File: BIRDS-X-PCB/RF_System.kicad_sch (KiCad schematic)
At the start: 44 parts, among them J1 SJ-43515TS, Q1 2N7000, Q2 2N7000, SW1 PTS645VL58-2 LFS, U1 MCP6004, U2 24LC32

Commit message: Clean up NucleoTNC
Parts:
- removed A1: NUCLEO-L432KC, KiCAD:MODULE_NUCLEO-L432KC, symbol NUCLEO-F303K8:NUCLEO-F303K8
- removed C10, C11: 0.1uF, Capacitor_THT:C_Disc_D3.4mm_W2.1mm_P2.50mm, symbol Device:C
- removed C12: 1uF, Capacitor_THT:C_Disc_D6.0mm_W2.5mm_P5.00mm, symbol Device:C
- removed C13: 10uF, Capacitor_THT:C_Disc_D6.0mm_W2.5mm_P5.00mm, symbol Device:C
- removed C3: 10nF, Capacitor_THT:C_Disc_D6.0mm_W2.5mm_P5.00mm, symbol Device:C
- removed C4, C9: 470pF, Capacitor_THT:C_Disc_D6.0mm_W2.5mm_P5.00mm, symbol Device:C
- removed C5, C8: 33nF, Capacitor_THT:C_Disc_D6.0mm_W2.5mm_P5.00mm, symbol Device:C
- removed H1, H2, H3, H4: MountingHole_Pad, MountingHole:MountingHole_3.2mm_M3_ISO14580_Pad, symbol Mechanical:MountingHole_Pad
- removed J1: SJ-43515TS, KiCAD:CUI_SJ-43515TS, symbol Connector:AudioJack4
- removed R10, R15: 16K, Resistor_THT:R_Axial_DIN0207_L6.3mm_D2.5mm_P7.62mm_Horizontal, symbol Device:R
- removed R12, R14: 510, Resistor_THT:R_Axial_DIN0207_L6.3mm_D2.5mm_P7.62mm_Horizontal, symbol Device:R
- removed R13, R6: 220, Resistor_THT:R_Axial_DIN0207_L6.3mm_D2.5mm_P7.62mm_Horizontal, symbol Device:R
- removed R16, R7: 30K, Resistor_THT:R_Axial_DIN0207_L6.3mm_D2.5mm_P7.62mm_Horizontal, symbol Device:R
- removed R17, R18, R4: 2K2, Resistor_THT:R_Axial_DIN0207_L6.3mm_D2.5mm_P7.62mm_Horizontal, symbol Device:R
- removed R2, R3: R470, Resistor_THT:R_Axial_DIN0207_L6.3mm_D2.5mm_P7.62mm_Horizontal, symbol Device:R
- removed R9: 100K, Resistor_THT:R_Axial_DIN0207_L6.3mm_D2.5mm_P7.62mm_Horizontal, symbol Device:R
- removed SW1: PTS645VL58-2 LFS, Button_Switch_THT:SW_Tactile_SPST_Angled_PTS645Vx58-2LFS, symbol Switch:SW_Push
- added C405 (x2): 33n, Capacitor_SMD:C_0603_1608Metric_Pad1.08x0.95mm_HandSolder, symbol Device:C
- added C405 (x2): 100n, Capacitor_SMD:C_0603_1608Metric_Pad1.08x0.95mm_HandSolder, symbol Device:C
- added C405: 10n, Capacitor_SMD:C_0603_1608Metric_Pad1.08x0.95mm_HandSolder, symbol Device:C
- added C405 (x2): 470p, Capacitor_SMD:C_0603_1608Metric_Pad1.08x0.95mm_HandSolder, symbol Device:C
- added R403 (x2): 30k, Resistor_SMD:R_0603_1608Metric_Pad0.98x0.95mm_HandSolder, symbol Device:R
- added R403 (x2): 470, Resistor_SMD:R_0603_1608Metric_Pad0.98x0.95mm_HandSolder, symbol Device:R
- added R403 (x2): 510, Resistor_SMD:R_0603_1608Metric_Pad0.98x0.95mm_HandSolder, symbol Device:R
- added R403 (x2): 16k, Resistor_SMD:R_0603_1608Metric_Pad0.98x0.95mm_HandSolder, symbol Device:R
- added R403: 100k, Resistor_SMD:R_0603_1608Metric_Pad0.98x0.95mm_HandSolder, symbol Device:R
- added R403: 2.2k, Resistor_SMD:R_0603_1608Metric_Pad0.98x0.95mm_HandSolder, symbol Device:R
- added R403 (x2): 220, Resistor_SMD:R_0603_1608Metric_Pad0.98x0.95mm_HandSolder, symbol Device:R
- U2: value 24LC32 -> 24LC32A/SN; footprint Package_DIP:DIP-8_W7.62mm_Socket -> Package_SO:SOP-8_3.9x4.9mm_P1.27mm; LCSC (none) -> C615215
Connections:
- net +3.3V: now also C405.1, C405.1
- net ADC_AUDIO: now also C405.1, R403.2
- net AUDIO_OUT: now also R403.1
- net DAC_AUDIO: now also R403.2
- net GND: now also C405.2, C405.2, C405.2, C405.2, C405.2, C405.2, C405.2
- net PTT_MULTIPLEX: now also R403.2
- net PTT_SIMPLEX: now also R403.2
- net at C7.1: now also R403.1, R403.2
- net at U1.3 (+): now also C405.1, R403.1
- net at C7.2, U1.1, U1.2 (-): now also R403.2
- net at C6.1, U1.13 (-), U1.14: now also R403.1
- net at U1.12 (+): now also C405.1, R403.2
- net at U1.8, U1.9 (-): now also R403.1
- net at Q2.2 (G), R11.1: now also R403.1
- net at Q1.3 (D): now also R403.2
- net at C6.2: now also R403.1, R403.2
- net at C2.2: now also R403.1
- net at R8.1, U1.5 (+): now also R403.1
- net at U1.6 (-), U1.7: now also R403.1, R403.2
- net at Q1.2 (G), R5.1: now also R403.1
- new net: C405.1, R403.2
- new net: C405.1, R403.1, R403.2
- no-connect marks 15 -> 0
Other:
- note added: "PERSISTENT CONFIGURATION - EEPROM"
- note added: "PTT = Push-to-Talk"
- note added: "TODO confirm if PTT is active high or low"
- note removed: "PERSISTENT CONFIGURATION"
- moved on the sheet: C2, C7, Q1, Q2, R11, R5, R8, U1A, U1B, U2

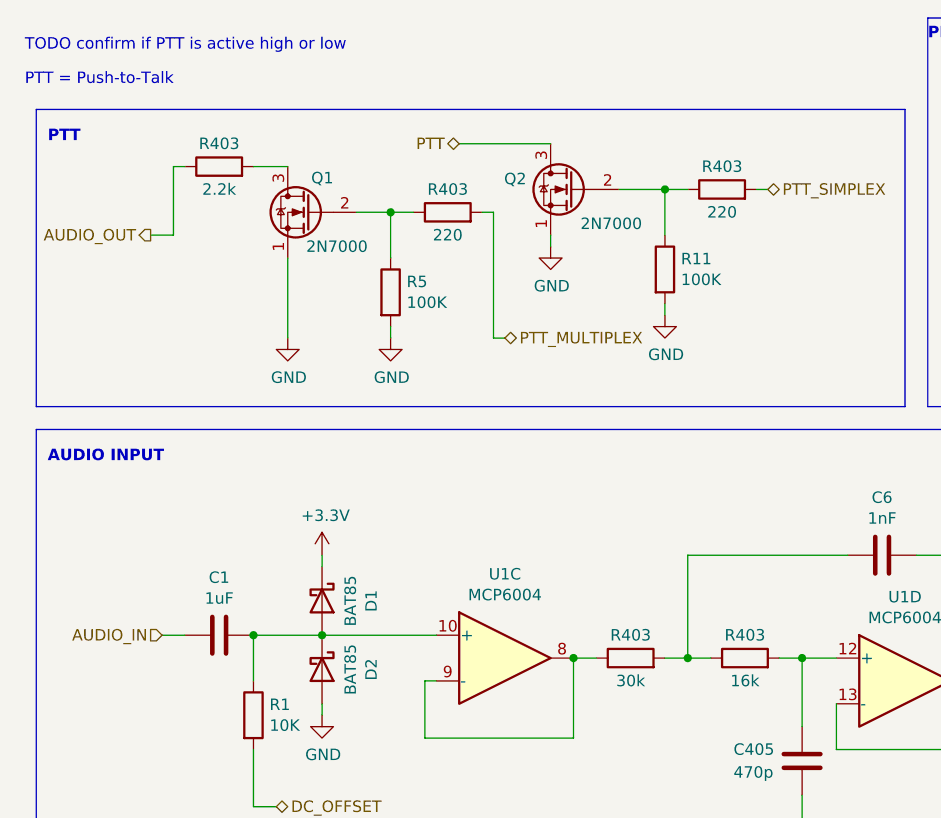
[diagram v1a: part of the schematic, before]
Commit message: Update parts in RF system
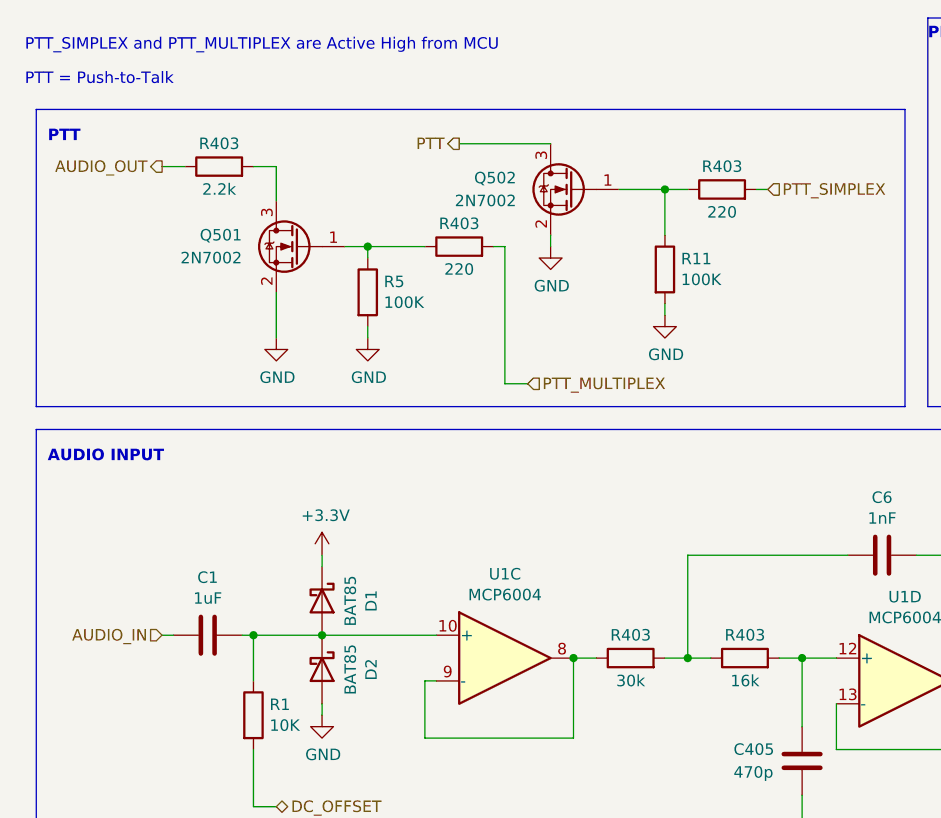
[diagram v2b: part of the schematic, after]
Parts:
- removed Q1, Q2: 2N7000, Package_TO_SOT_THT:TO-92_Inline, symbol Transistor_FET:2N7000
- added Q501, Q502: 2N7002, Package_TO_SOT_THT:TO-92_Inline, symbol Transistor_FET:2N7002
- C1, C2, C6, C7: footprint Capacitor_THT:C_Disc_D6.0mm_W2.5mm_P5.00mm -> Capacitor_SMD:C_0603_1608Metric_Pad1.08x0.95mm_HandSolder
- R1, R11, R5, R8: footprint Resistor_THT:R_Axial_DIN0207_L6.3mm_D2.5mm_P7.62mm_Horizontal -> Resistor_SMD:R_0603_1608Metric_Pad0.98x0.95mm_HandSolder
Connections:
- net GND: now also Q501.2 (S), Q502.2 (S)
- net PTT: now also Q502.3 (D)
- net at R11.1, R403.1: now also Q502.1 (G)
- net at R403.2: now also Q501.3 (D)
- net at R403.1, R5.1: now also Q501.1 (G)
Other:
- note added: "PTT_SIMPLEX and PTT_MULTIPLEX are Active High from MCU"
- note removed: "TODO confirm if PTT is active high or low"
- moved on the sheet: C1, R403, R5

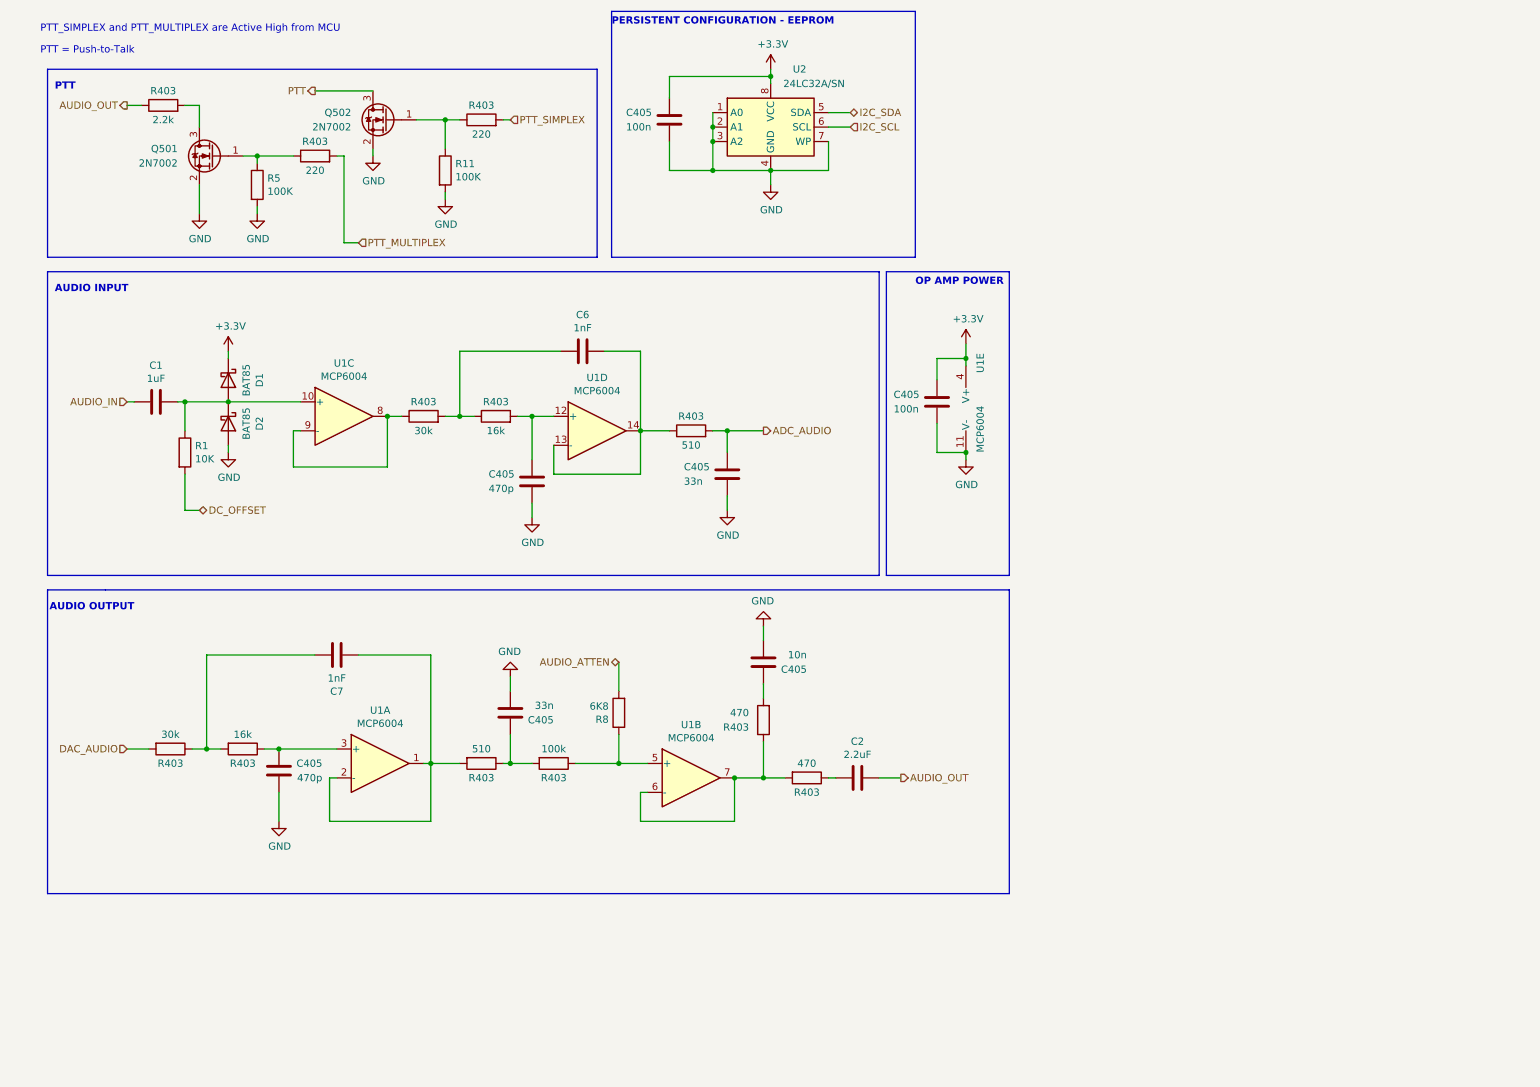
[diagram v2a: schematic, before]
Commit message: Add DRA818V content
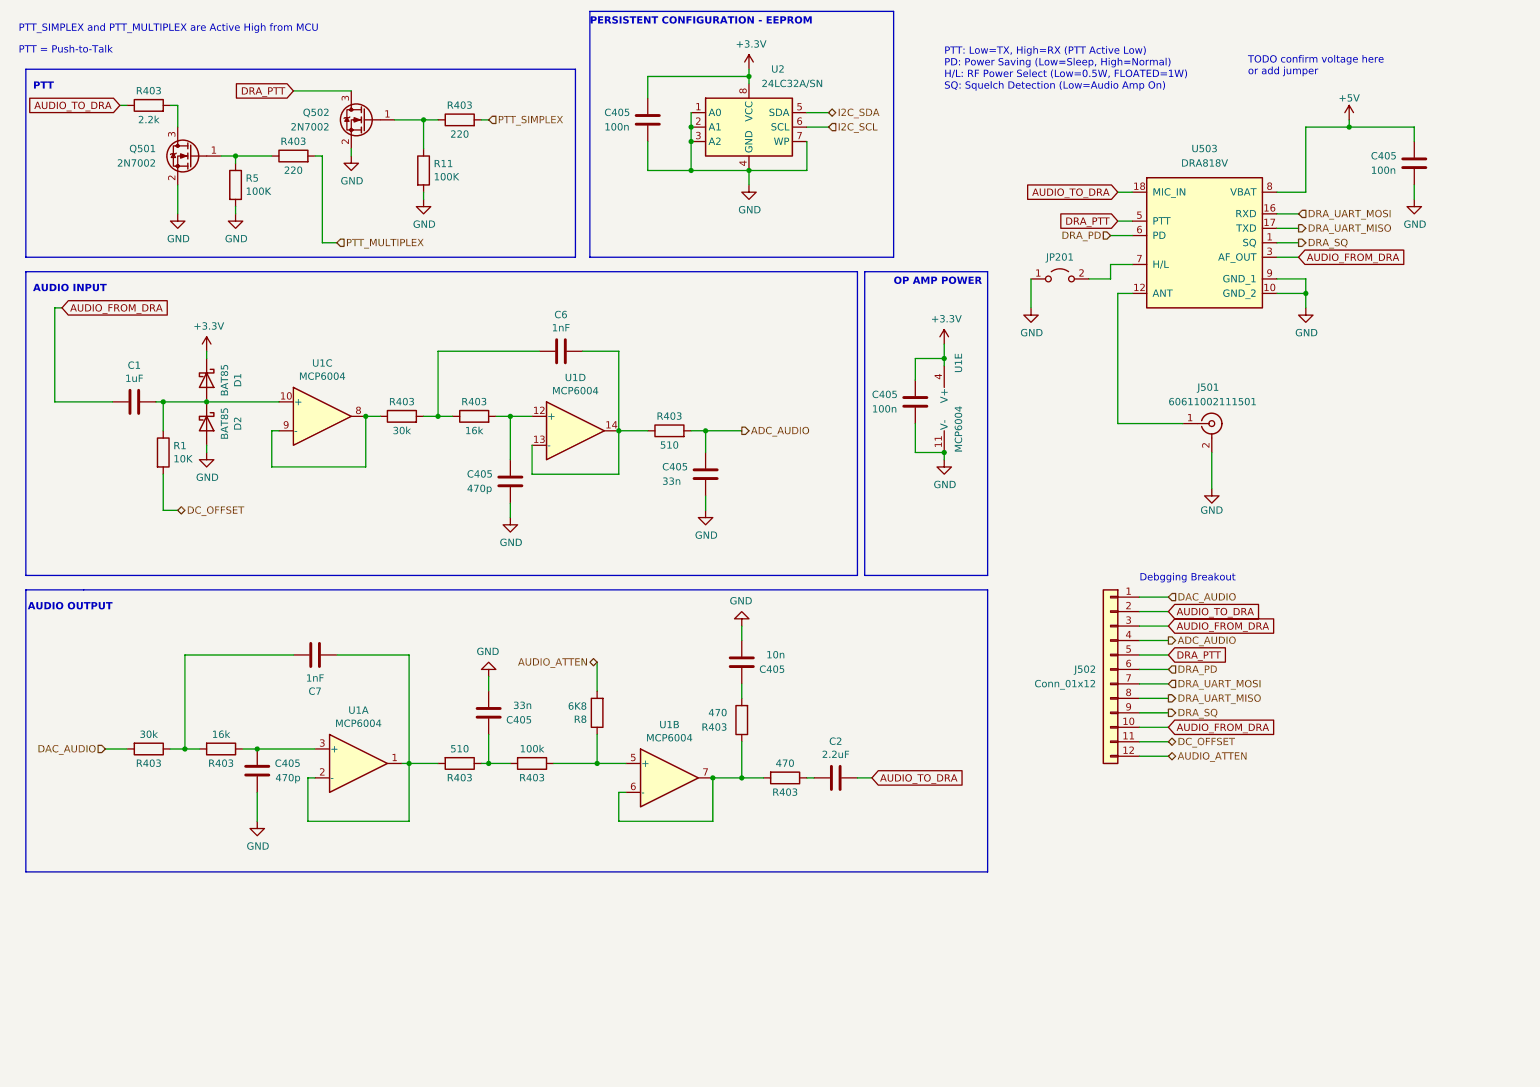
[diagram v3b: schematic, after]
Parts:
- added C405: 100n, Capacitor_SMD:C_0603_1608Metric_Pad1.08x0.95mm_HandSolder, symbol Device:C
- added J501: 60611002111501, Connector_Coaxial:SMA_Amphenol_901-143_Horizontal, symbol Connector:Conn_Coaxial
- added J502: Conn_01x12, symbol Connector_Generic:Conn_01x12
- added JP201: Jumper_2_Open, Jumper:SolderJumper-2_P1.3mm_Open_RoundedPad1.0x1.5mm, symbol Jumper:Jumper_2_Open
- added U503: DRA818V, BIRDS-X_Footprints_Lib:DORJI_DRA818V, symbol BIRDS-X_Symbols_Lib:DRA818V
- Q501, Q502: LCSC C282260 -> C3290044
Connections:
- net ADC_AUDIO: now also J502.4 (Pin_4)
- net AUDIO_ATTEN: now also J502.12 (Pin_12)
- net DAC_AUDIO: now also J502.1 (Pin_1)
- net DC_OFFSET: now also J502.11 (Pin_11)
- net GND: now also C405.2, J501.2 (Ext), JP201.1 (A), U503.10 (GND_2), U503.9 (GND_1)
- net AUDIO_IN renamed AUDIO_FROM_DRA
- net AUDIO_FROM_DRA: now also J502.10 (Pin_10), J502.3 (Pin_3), U503.3 (AF_OUT)
- net AUDIO_OUT renamed AUDIO_TO_DRA
- net AUDIO_TO_DRA: now also J502.2 (Pin_2), U503.18 (MIC_IN)
- net PTT renamed DRA_PTT
- net DRA_PTT: now also J502.5 (Pin_5), U503.5 (PTT)
- new net: J501.1 (In), U503.12 (ANT)
- new net: JP201.2 (B), U503.7 (H/L)
- new net +5V: C405.1, U503.8 (VBAT)
- new net DRA_PD: J502.6 (Pin_6), U503.6 (PD)
- new net DRA_SQ: J502.9 (Pin_9), U503.1 (SQ)
- new net DRA_UART_MISO: J502.8 (Pin_8), U503.17 (TXD)
- new net DRA_UART_MOSI: J502.7 (Pin_7), U503.16 (RXD)
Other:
- note added: "Debgging Breakout"
- note added: "PTT: Low=TX, High=RX (PTT Active Low) PD: Power Saving (Low=Sleep, High=Normal) H/L: RF Power Select (Low=0.5W, FLOATED=1W) SQ: Squelch Detection (Low=Audio Amp On)"
- note added: "TODO confirm voltage here or add jumper"
- moved on the sheet: C1, C2, C405, C6, C7, D1, D2, Q501, Q502, R1, R11, R403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

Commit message: Finish double MCU re-org
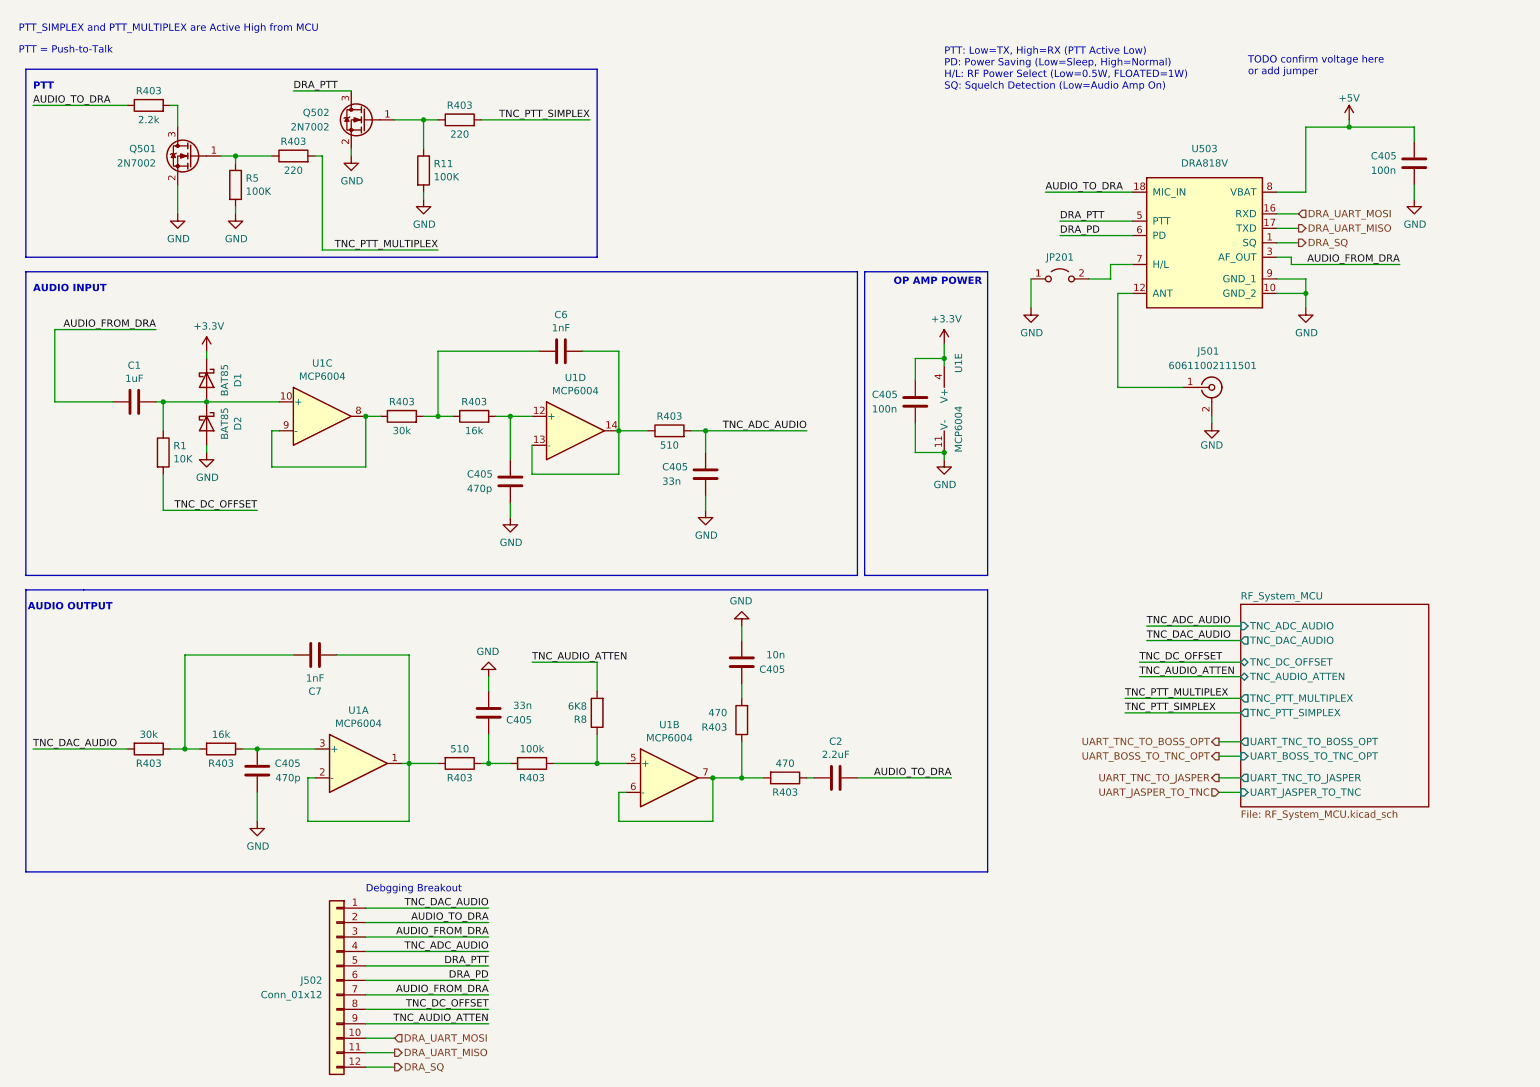
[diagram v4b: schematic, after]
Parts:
- removed C405: 100n, Capacitor_SMD:C_0603_1608Metric_Pad1.08x0.95mm_HandSolder, symbol Device:C
- removed U2: 24LC32A/SN, Package_SO:SOP-8_3.9x4.9mm_P1.27mm, symbol Memory_EEPROM:24LC32
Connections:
- net AUDIO_FROM_DRA: now also J502.7 (Pin_7); no longer J502.10 (Pin_10)
- net DRA_SQ: now also J502.12 (Pin_12); no longer J502.9 (Pin_9)
- net DRA_UART_MISO: now also J502.11 (Pin_11); no longer J502.8 (Pin_8)
- net DRA_UART_MOSI: now also J502.10 (Pin_10); no longer J502.7 (Pin_7)
- net ADC_AUDIO renamed TNC_ADC_AUDIO
- net AUDIO_ATTEN renamed TNC_AUDIO_ATTEN
- net TNC_AUDIO_ATTEN: now also J502.9 (Pin_9); no longer J502.12 (Pin_12)
- net DAC_AUDIO renamed TNC_DAC_AUDIO
- net DC_OFFSET renamed TNC_DC_OFFSET
- net TNC_DC_OFFSET: now also J502.8 (Pin_8); no longer J502.11 (Pin_11)
- net PTT_MULTIPLEX renamed TNC_PTT_MULTIPLEX
- net PTT_SIMPLEX renamed TNC_PTT_SIMPLEX
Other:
- added sheet RF_System_MCU (RF_System_MCU.kicad_sch)
- note removed: "PERSISTENT CONFIGURATION - EEPROM"
- moved on the sheet: J501, J502

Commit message: Clean up heirarchy
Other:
- sheet RF_System_MCU ports: added none; removed UART_BOSS_TO_TNC_OPT, UART_TNC_TO_BOSS_OPT
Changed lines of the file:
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@@
-    (stroke (width 0) (type default))
-  )
-  (wire (pts (xy 224.79 146.05) (xy 228.6 146.05))
     (stroke (width 0) (type default))
   )
@@
   )
   (wire (pts (xy 205.74 62.23) (xy 205.74 59.69))
-    (stroke (width 0) (type default))
-  )
-  (wire (pts (xy 224.79 143.51) (xy 228.6 143.51))
     (stroke (width 0) (type default))
   )
@@
     (effects (font (size 1.27 1.27)) (justify left))
   )
-  (hierarchical_label "UART_TNC_TO_BOSS_OPT" (shape output) (at 224.79 143.51 180) (fields_autoplaced)
-    (effects (font (size 1.27 1.27)) (justify right))
-  )
   (hierarchical_label "DRA_UART_MISO" (shape output) (at 238.76 53.34 0) (fields_autoplaced)
     (effects (font (size 1.27 1.27)) (justify left))
-  )
-  (hierarchical_label "UART_BOSS_TO_TNC_OPT" (shape output) (at 224.79 146.05 180) (fields_autoplaced)
-    (effects (font (size 1.27 1.27)) (justify right))
   )
   (hierarchical_label "UART_TNC_TO_JASPER" (shape output) (at 224.79 149.86 180) (fields_autoplaced)
@@
       (effects (font (size 1.27 1.27)) (justify left))
     )
-    (pin "UART_TNC_TO_BOSS_OPT" output (at 228.6 143.51 180)
-      (effects (font (size 1.27 1.27)) (justify left))
-    )
-    (pin "UART_BOSS_TO_TNC_OPT" input (at 228.6 146.05 180)
-      (effects (font (size 1.27 1.27)) (justify left))
-    )
